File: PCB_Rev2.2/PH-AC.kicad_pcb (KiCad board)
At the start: 2 copper layers, 200 x 100 mm, 51 parts, among them J1 USB_C_Receptacle_USB2.0_14P, J2 Conn_01x03, SW1 SW_Push, SW10 SW_Push, SW2 RotaryEncoder_Switch_MP, SW3 RotaryEncoder_Switch_MP, SW4 SW_Push, SW5 SW_Push, SW6 SW_Push, SW7 SW_Push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

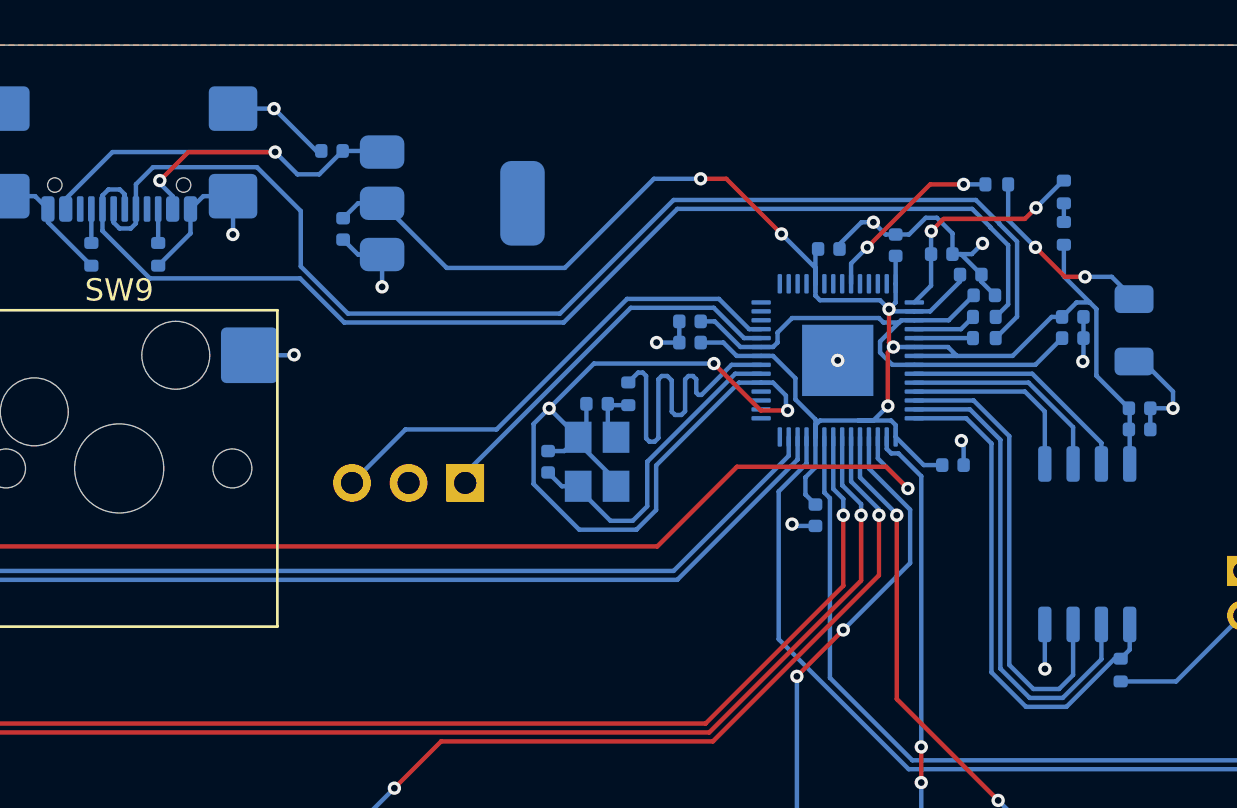
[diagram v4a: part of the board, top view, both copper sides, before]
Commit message: Still Tinkering
Changed the package of 27ohm resistor from 0402 to 0603 to avoid extra expenses

Changed the capacitance of C17 and C18 from 15p to 20p to match the new 12Mhz crystal
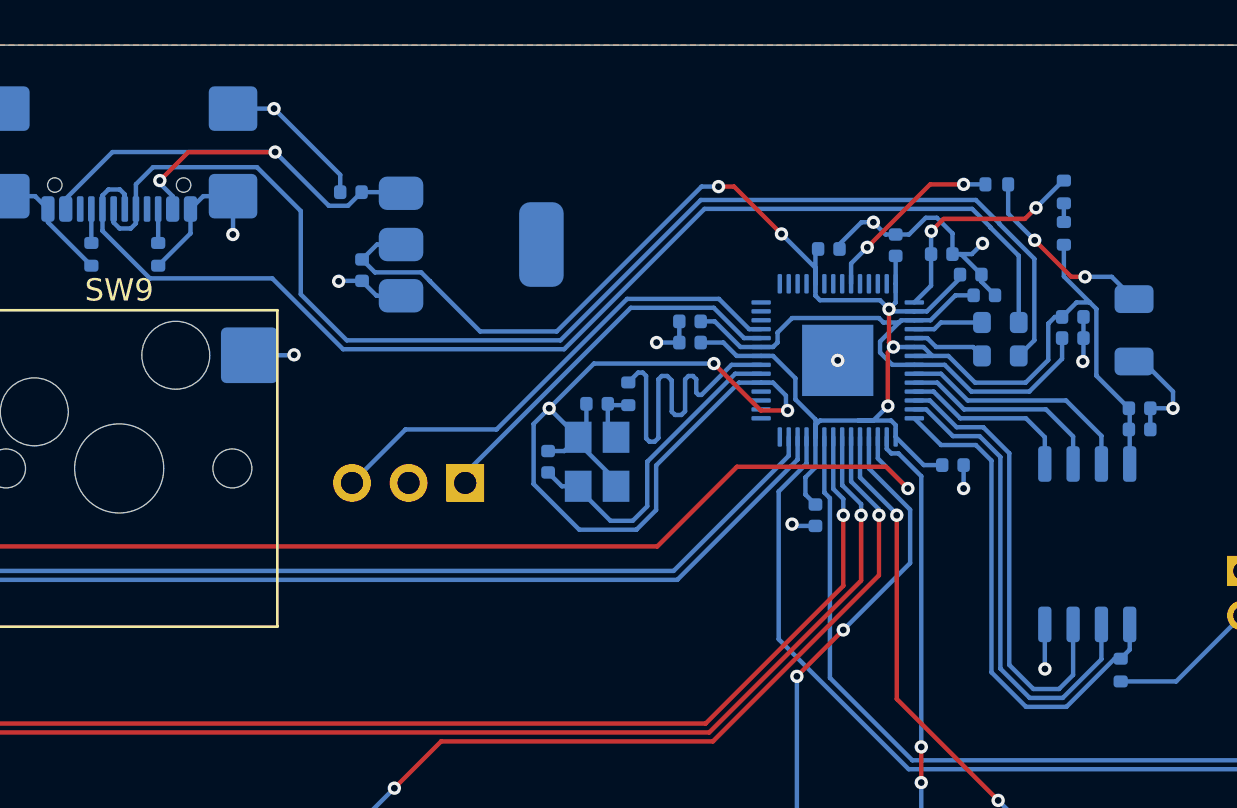
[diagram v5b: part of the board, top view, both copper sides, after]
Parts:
- C17, C18: value 15p -> 20p
- R14, R15: value 56K -> 5K1
- R3, R4: footprint Resistor_SMD:R_0402_1005Metric -> Resistor_SMD:R_0603_1608Metric
- moved U2 2.04 mm to (183.3, 62.0)
- moved C12 2.04 mm to (177.9, 59.6)
- moved C13 2.04 mm to (178.4, 63.1)
- moved R3 1.08 mm to (207.1, 67.0)
- moved R4 0.76 mm to (207.1, 65.5)
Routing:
- net /USB_DP: track 55.2 -> 58.0 mm
- net +3V3: track 86.9 -> 89.5 mm
- net GND: track 105.7 -> 107.3 mm
- net +1V1: track 25.0 -> 26.5 mm
- net VBUS: track 23.6 -> 24.9 mm
- net /USB_DM: track 52.7 -> 53.9 mm
- net Net-(U1-USB_DP): track 2.63 -> 3.37 mm
- net /QSPI_SD0: track 8.58 -> 7.91 mm

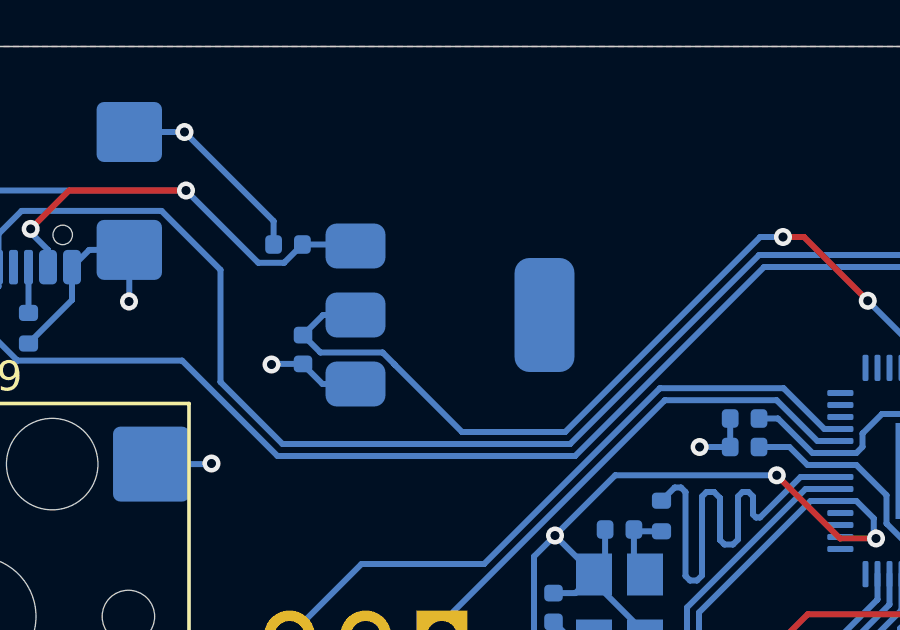
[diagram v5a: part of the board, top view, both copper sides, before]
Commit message: LDO Replacement
Changed NCP1117-3.3 to AMS1117-3.3 to avoid extra expenses, again
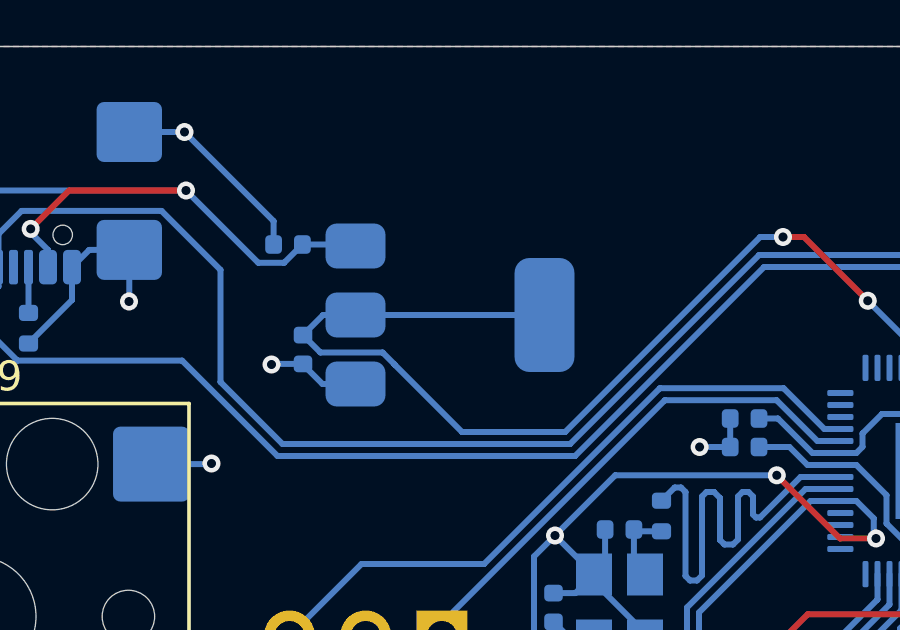
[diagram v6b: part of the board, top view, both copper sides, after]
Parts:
- J1: value USB_C_Receptacle_USB2.0_14P -> USB_C_Receptacle_USB2.0_16P
- U2: value NCP1117-3.3_SOT223 -> AMS1117-3.3; footprint Package_TO_SOT_SMD:SOT-223 -> Package_TO_SOT_SMD:SOT-223-3_TabPin2
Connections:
- J1 pad A8: (no net) -> unconnected-(J1-SBU1-PadA8)
- J1 pad B8: (no net) -> unconnected-(J1-SBU2-PadB8)
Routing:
- net +3V3: track 89.5 -> 95.8 mm
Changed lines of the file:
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@@
 	(net 59 "BT5")
 	(net 60 "BT6")
+	(net 61 "unconnected-(J1-SBU2-PadB8)")
+	(net 62 "unconnected-(J1-SBU1-PadA8)")
 	(footprint "PCM_Switch_Keyboard_Hotswap_Kailh:SW_Hotswap_Kailh_MX_1.50u"
 		(layer "F.Cu")
@@
 		)
 	)
-	(footprint "Package_TO_SOT_SMD:SOT-223"
+	(footprint "Package_TO_SOT_SMD:SOT-223-3_TabPin2"
 		(layer "B.Cu")
 		(at 183.3 61.95)
@@
 		(tags "CMS SOT")
 		(property "Reference" "U2"
-			(at 0 4.5 0)
+			(at 0 4.5 180)
 			(layer "B.SilkS")
 			(effects
@@
 			)
 		)
-		(property "Value" "NCP1117-3.3_SOT223"
-			(at 0 -4.5 0)
+		(property "Value" "AMS1117-3.3"
+			(at 0 -4.5 180)
 			(layer "B.Fab")
 			(effects
@@
 			)
 		)
-		(property "Footprint" "Package_TO_SOT_SMD:SOT-223"
+		(property "Footprint" "Package_TO_SOT_SMD:SOT-223-3_TabPin2"
 			(at 0 0 180)
 			(unlocked yes)
@@
 			)
 		)
-		(property "Datasheet" "http://www.onsemi.com/pub_link/Collateral/NCP1117-D.PDF"
+		(property "Datasheet" "http://www.advanced-monolithic.com/pdf/ds1117.pdf"
 			(at 0 0 180)
 			(unlocked yes)
@@
 			)
 		)
-		(property "Description" "1A Low drop-out regulator, Fixed Output 3.3V, SOT-223"
+		(property "Description" "1A Low Dropout regulator, positive, 3.3V fixed output, SOT-223"
 			(at 0 0 180)
 			(unlocked yes)
@@
 		(fp_line
 			(start -1.85 -3.35)
-			(end -1.85 2.3)
+			(end -1.85 2.35)
 			(stroke
 				(width 0.1)
@@
 		)
 		(fp_line
-			(start -0.8 3.35)
-			(end -1.85 2.3)
+			(start -0.85 3.35)
+			(end -1.85 2.35)
 			(stroke
 				(width 0.1)
@@
 		(fp_line
 			(start 1.85 3.35)
-			(end -0.8 3.35)
+			(end -0.85 3.35)
 			(stroke
 				(width 0.1)
@@
 		)
 		(fp_text user "${REFERENCE}"
-			(at 0 0 90)
+			(at 0 0 -90)
 			(layer "B.Fab")
 			(effects
@@
 			(pintype "power_out")
 		)
+		(pad "2" smd roundrect
+			(at 3.15 0)
+			(size 2 3.8)
+			(layers "B.Cu" "B.Paste" "B.Mask")
+			(roundrect_rratio 0.25)
+			(net 1 "+3V3")
+			(pinfunction "VO")
+			(pintype "power_out")
+		)
 		(pad "3" smd roundrect
 			(at -3.15 -2.3)
@@
 			(pintype "power_in")
 		)
-		(pad "4" smd roundrect
-			(at 3.15 0)
-			(size 2 3.8)
-			(layers "B.Cu" "B.Paste" "B.Mask")
-			(roundrect_rratio 0.25)
-		)
 		(model "${KICAD8_3DMODEL_DIR}/Package_TO_SOT_SMD.3dshapes/SOT-223.wrl"
 			(offset
@@
 			)
 		)
-		(property "Value" "USB_C_Receptacle_USB2.0_14P"
+		(property "Value" "USB_C_Receptacle_USB2.0_16P"
 			(at 0 -5 180)
 			(unlocked yes)
@@
 			)
 		)
-		(property "Description" "USB 2.0-only 14P Type-C Receptacle connector"
+		(property "Description" "USB 2.0-only 16P Type-C Receptacle connector"
 			(at 0 0 180)
 			(unlocked yes)
@@
 			(layers "B.Cu" "B.Paste" "B.Mask")
 			(roundrect_rratio 0.25)
+			(net 62 "unconnected-(J1-SBU1-PadA8)")
+			(pinfunction "SBU1")
+			(pintype "bidirectional+no_connect")
 			(thermal_bridge_angle 45)
 		)
@@
 			(layers "B.Cu" "B.Paste" "B.Mask")
 			(roundrect_rratio 0.25)
+			(net 61 "unconnected-(J1-SBU2-PadB8)")
+			(pinfunction "SBU2")
+			(pintype "bidirectional+no_connect")
 			(thermal_bridge_angle 45)
 		)
@@
 		(width 0.2)
 		(layer "B.Cu")
+		(net 1)
+	)
+	(segment
+		(start 180.15 61.95)
+		(end 186.45 61.95)
+		(width 0.2)
+		(layer "B.Cu")

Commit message: Redesign
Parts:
- removed C17, C18: 20p, Capacitor_SMD:C_0402_1005Metric
- removed D2: LED, LED_SMD:LED_1206_3216Metric
- removed J2: Conn_01x03, Connector_PinHeader_2.54mm:PinHeader_1x03_P2.54mm_Vertical
- removed R12, R9: 1K, Resistor_SMD:R_0402_1005Metric
- removed R13: 470R, Resistor_SMD:R_0402_1005Metric
- removed R14, R15: 5K1, Resistor_SMD:R_0402_1005Metric
- removed R2: 200R, Resistor_SMD:R_0402_1005Metric
- added C16: 100n, Capacitor_SMD:C_0402_1005Metric, B.Cu at (146.4, 67.5)
- added R5: 1K, Resistor_SMD:R_0402_1005Metric, B.Cu at (129.2, 70.8)
- added R6: 5K1, Resistor_SMD:R_0402_1005Metric, B.Cu at (165.8, 63.0)
- added R7: 5K1, Resistor_SMD:R_0402_1005Metric, B.Cu at (169.2, 63.0)
- C1, C4: value 100n -> 10u
- C10: value 2u2 -> 1u
- C11, C14, C9: value 2u2 -> 100n
- C12, C13: value 10u -> 100n
- C2, C3: value 100n -> 20p
- C8: value 100n -> 1u
- R1: value 1R -> 1K
- moved C2 81.7 mm to (129.2, 75.2), turned to 180 degrees
- moved C7 75.8 mm to (134.7, 71.3), turned to 90 degrees
- moved C15 74.3 mm to (139.5, 79.0), turned to -90 degrees
- moved C14 69.2 mm to (144.8, 78.5), turned to -90 degrees
- moved C3 67.0 mm to (126.5, 73.0), turned to -90 degrees
- moved R1 62.5 mm to (151.8, 82.5), turned to 180 degrees
- moved C11 61.0 mm to (143.6, 67.5), turned to 90 degrees
- moved Y1 59.7 mm to (129.2, 73.0), turned to 180 degrees
- moved C4 59.5 mm to (146.4, 61.1), turned to 90 degrees
- moved U3 59.3 mm to (151.8, 79.0), turned to 0 degrees
- moved U1 59.0 mm to (141.0, 72.8)
- moved R3 58.5 mm to (148.8, 71.2)
- moved R4 58.5 mm to (148.8, 69.8)
- moved C9 57.8 mm to (149.2, 73.5), turned to -90 degrees
- moved C10 57.1 mm to (148.8, 67.5)
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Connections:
- net /USB_DM renamed /USB_DN
- C1 pad 1: +3V3 -> VBUS
- C11 pad 1: Net-(U1-ADC_AVDD) -> +3V3
- C12 pad 1: VBUS -> +3V3
- C2 pad 1: +3V3 -> /XIN
- C3 pad 1: +3V3 -> Net-(C3-Pad1)
- C6 pad 1: +3V3 -> +1V1
- C9 pad 1: +1V1 -> +3V3
- R1 pad 2: Net-(U1-ADC_AVDD) -> /QSPI_SS
- SW1 pad 2: Net-(R9-Pad1) -> Net-(R1-Pad1)
- U1 pad 24: Net-(J2-Pin_1) -> unconnected-(U1-SWCLK-Pad24)
- U1 pad 25: Net-(J2-Pin_3) -> unconnected-(U1-SWD-Pad25)
- U1 pad 37: Net-(U1-GPIO25) -> unconnected-(U1-GPIO25-Pad37)
- U1 pad 43: Net-(U1-ADC_AVDD) -> +3V3
- Y1 pad 3: Net-(C18-Pad1) -> Net-(C3-Pad1)
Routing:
- net ENC2A: track 134.8 -> 67.1 mm
- net BT0: track 105.3 -> 39.8 mm, vias 2 -> 0
- net ENC2B: track 126.9 -> 65.9 mm
- net BT1: track 74.1 -> 18.4 mm, vias 2 -> 0
- net BT4: track 125.5 -> 70.5 mm
- net ENC1A: track 64.1 -> 119.1 mm, vias 0 -> 1
- net ENC1B: track 64.1 -> 118.7 mm, vias 0 -> 1
- net BT3: track 26.8 -> 80.5 mm, vias 2 -> 0
- net /USB_DP: track 58.0 -> 27.9 mm, vias 0 -> 2
- net /USB_DN: track 53.9 -> 26.8 mm, vias 0 -> 2
- net BT6: track 70.0 -> 94.5 mm
- net Net-(J2-Pin_3): track 22.3 -> 0.00 mm
- net Net-(J2-Pin_1): track 17.4 -> 0.00 mm
- net +3V3: track 95.8 -> 112.9 mm, vias 5 -> 0
- net BT5: track 58.2 -> 43.3 mm, vias 2 -> 0
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
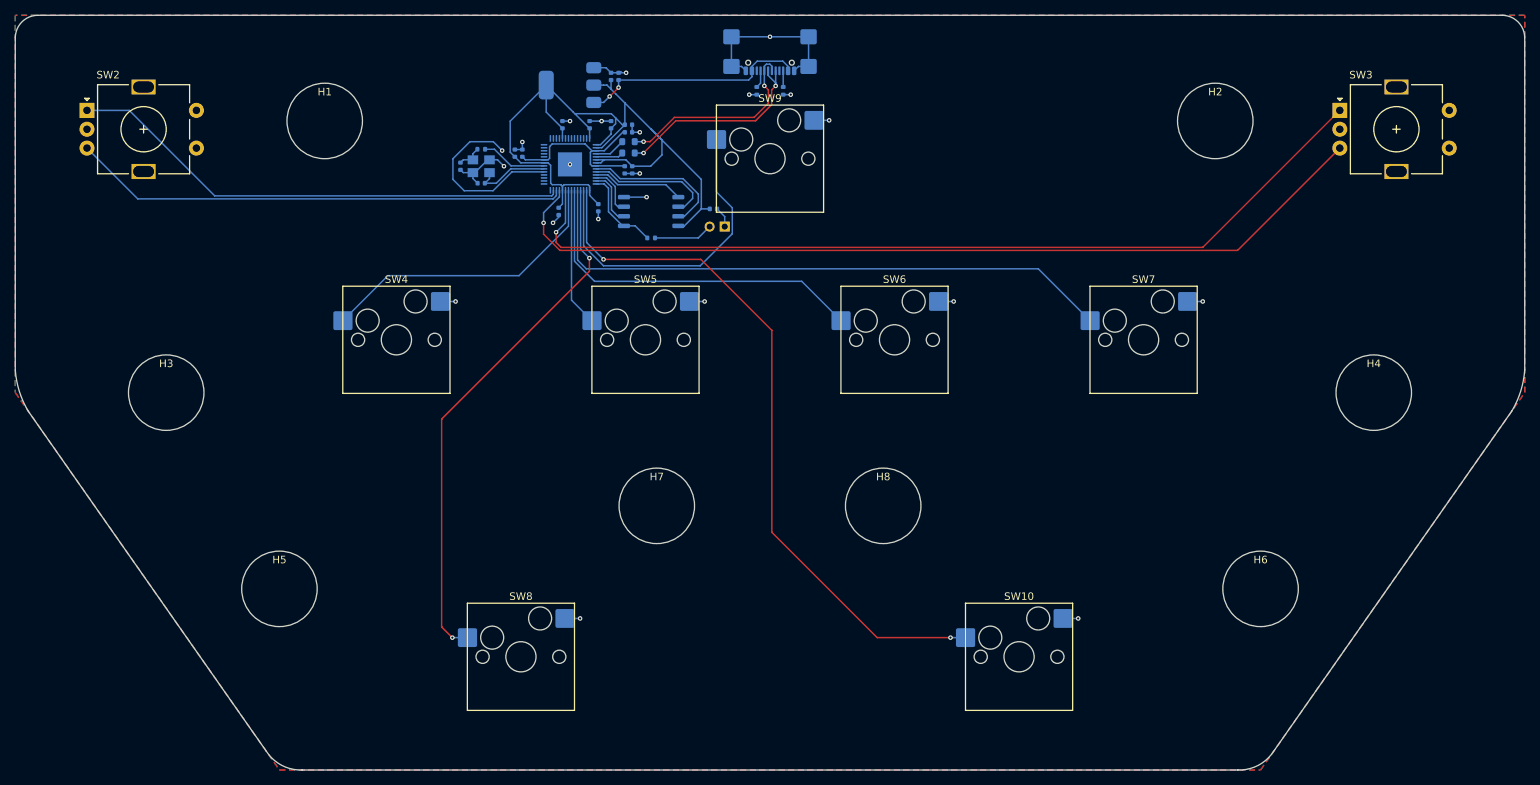
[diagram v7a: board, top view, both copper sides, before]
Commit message: Revert "Redesign"
This reverts commit 8763a19c73a96b1086359286b52022891444512d.
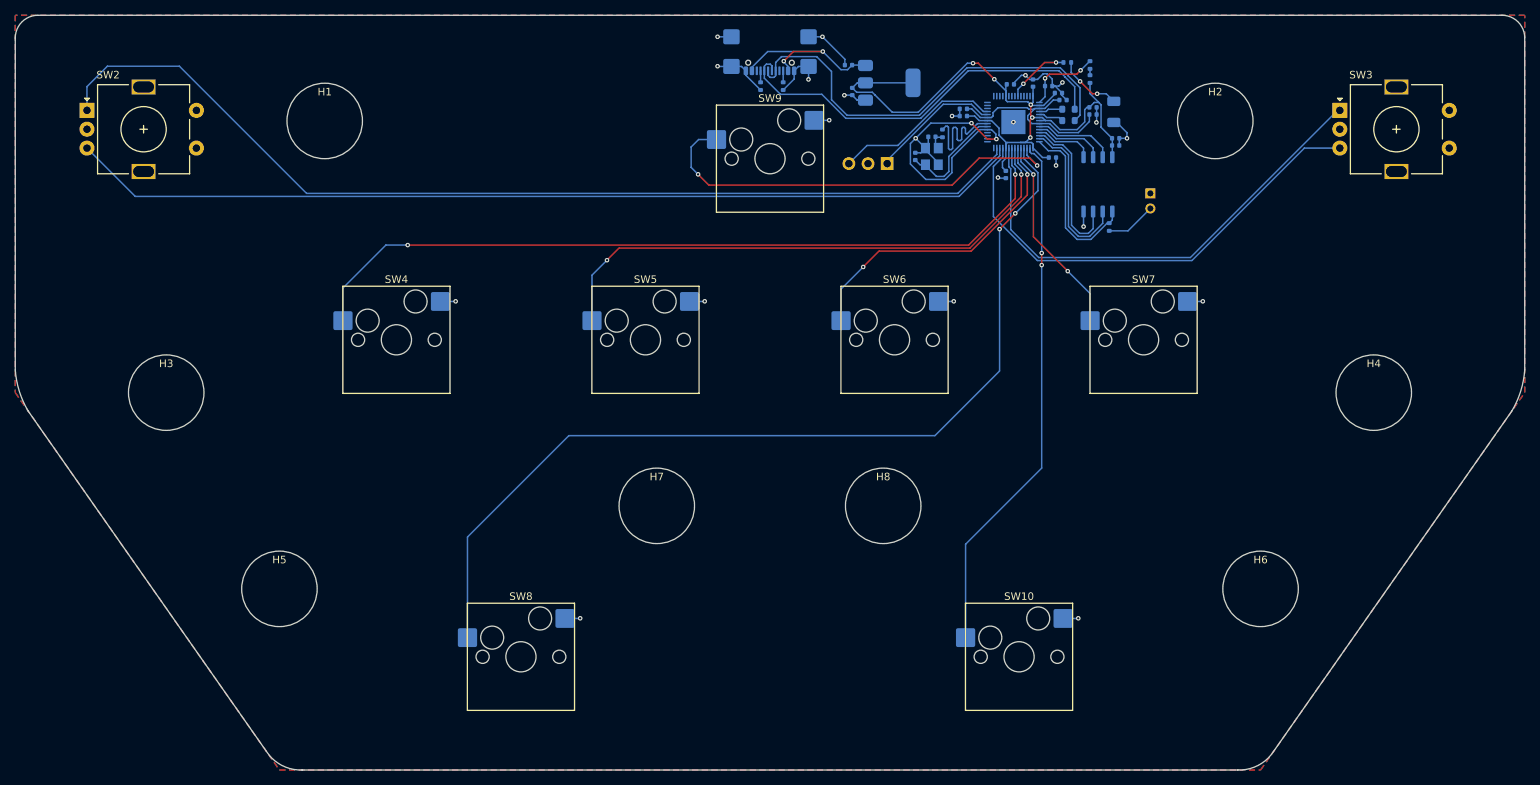
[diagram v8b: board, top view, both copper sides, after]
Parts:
- removed C16: 100n, Capacitor_SMD:C_0402_1005Metric
- removed R5: 1K, Resistor_SMD:R_0402_1005Metric
- removed R6, R7: 5K1, Resistor_SMD:R_0402_1005Metric
- added C17: 20p, Capacitor_SMD:C_0402_1005Metric, B.Cu at (186.8, 71.7)
- added C18: 20p, Capacitor_SMD:C_0402_1005Metric, B.Cu at (188.9, 69.1)
- added D2: LED, LED_SMD:LED_1206_3216Metric, B.Cu at (213.1, 65.8)
- added J2: Conn_01x03, Connector_PinHeader_2.54mm:PinHeader_1x03_P2.54mm_Vertical, B.Cu at (183.0, 72.7)
- added R12: 1K, Resistor_SMD:R_0402_1005Metric, B.Cu at (190.3, 68.7)
- added R13: 470R, Resistor_SMD:R_0402_1005Metric, B.Cu at (206.9, 59.2)
- added R14: 5K1, Resistor_SMD:R_0402_1005Metric, B.Cu at (166.2, 62.4)
- added R15: 5K1, Resistor_SMD:R_0402_1005Metric, B.Cu at (169.2, 62.4)
- added R2: 200R, Resistor_SMD:R_0402_1005Metric, B.Cu at (209.9, 61.5)
- added R9: 1K, Resistor_SMD:R_0402_1005Metric, B.Cu at (212.4, 81.0)
- C1, C4: value 10u -> 100n
- C10: value 1u -> 2u2
- C11, C14, C9: value 100n -> 2u2
- C12, C13: value 100n -> 10u
- C2, C3: value 20p -> 100n
- C8: value 1u -> 100n
- R1: value 1K -> 1R
- moved C2 81.7 mm to (210.3, 65.2), turned to 0 degrees
- moved C7 75.8 mm to (210.3, 66.2), turned to 0 degrees
- moved C15 74.3 mm to (213.3, 70.2), turned to 0 degrees
- moved C14 69.2 mm to (213.3, 69.3), turned to 0 degrees
- moved C3 67.0 mm to (193.1, 66.3), turned to 180 degrees
- moved R1 62.5 mm to (209.9, 59.6), turned to 90 degrees
- moved C11 61.0 mm to (204.4, 62.4), turned to 0 degrees
- moved Y1 59.7 mm to (188.9, 71.7), turned to 90 degrees
- moved C4 59.5 mm to (204.9, 71.8), turned to 0 degrees
- moved U3 59.3 mm to (210.9, 75.4), turned to 90 degrees
- moved U1 59.0 mm to (199.8, 67.2)
- moved R3 58.5 mm to (207.1, 67.0)
- moved R4 58.5 mm to (207.1, 65.5)
- moved C9 57.8 mm to (206.3, 64.2), turned to 0 degrees
- moved C10 57.1 mm to (205.7, 63.3)
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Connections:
- net /USB_DN renamed /USB_DM
- C1 pad 1: VBUS -> +3V3
- C11 pad 1: +3V3 -> Net-(U1-ADC_AVDD)
- C12 pad 1: +3V3 -> VBUS
- C2 pad 1: /XIN -> +3V3
- C3 pad 1: Net-(C3-Pad1) -> +3V3
- C6 pad 1: +1V1 -> +3V3
- C9 pad 1: +3V3 -> +1V1
- R1 pad 2: /QSPI_SS -> Net-(U1-ADC_AVDD)
- SW1 pad 2: Net-(R1-Pad1) -> Net-(R9-Pad1)
- U1 pad 24: unconnected-(U1-SWCLK-Pad24) -> Net-(J2-Pin_1)
- U1 pad 25: unconnected-(U1-SWD-Pad25) -> Net-(J2-Pin_3)
- U1 pad 37: unconnected-(U1-GPIO25-Pad37) -> Net-(U1-GPIO25)
- U1 pad 43: +3V3 -> Net-(U1-ADC_AVDD)
- Y1 pad 3: Net-(C3-Pad1) -> Net-(C18-Pad1)
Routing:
- net ENC2A: track 67.1 -> 134.8 mm
- net BT0: track 39.8 -> 105.3 mm, vias 0 -> 2
- net ENC2B: track 65.9 -> 126.9 mm
- net BT1: track 18.4 -> 74.1 mm, vias 0 -> 2
- net BT4: track 70.5 -> 125.5 mm
- net ENC1A: track 119.1 -> 64.1 mm, vias 1 -> 0
- net ENC1B: track 118.7 -> 64.1 mm, vias 1 -> 0
- net BT3: track 80.5 -> 26.8 mm, vias 0 -> 2
- net /USB_DP: track 27.9 -> 58.0 mm, vias 2 -> 0
- net /USB_DM: track 26.8 -> 53.9 mm, vias 2 -> 0
- net BT6: track 94.5 -> 70.0 mm
- net Net-(J2-Pin_3): track 0.00 -> 22.3 mm
- net Net-(J2-Pin_1): track 0.00 -> 17.4 mm
- net +3V3: track 112.9 -> 95.8 mm, vias 0 -> 5
- net BT5: track 43.3 -> 58.2 mm, vias 0 -> 2
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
